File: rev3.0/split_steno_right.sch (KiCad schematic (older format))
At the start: 37 parts, among them J1 USB_B, J2 Audio-Jack-4, J3 Conn_02x04_Odd_Even, J4 Conn_01x03, J5 Conn_01x03, J6 Conn_01x02, P1 TC2030-IDC, SW1 SW_Push, SW10 SW_Push, SW11 SW_Push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

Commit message: filled gnd plane on left
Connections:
- net KEY1: no longer U2.24 (PD4/OC1A/~SS~)
- net KEY10: no longer U2.43 (AC3/ADC3/PA3)
- net KEY11: no longer U2.11 (SCLIN/SCL/XCK0/OC0AHS/OC0B/PC1)
- net KEY12: no longer U2.10 (SDAIN/SDA/~OC0ALS~/OC0A/PC0)
- net KEY13: no longer U2.3 (AC0OUT/AC7/ADC7/PA7)
- net KEY14: no longer U2.2 (AC1OUT/AC6/ADC6/PA6)
- net KEY15: no longer U2.44 (AC4/ADC4/PA4)
- net KEY16: no longer U2.5 (ADC9/PB1)
- net KEY17: no longer U2.4 (AREFB/ADC8/PB0)
- net KEY18: no longer U2.1 (AC5/ADC5/PA5)
- net KEY2: no longer U2.25 (PD5/OC1B/XCK1/MOSI)
- net KEY3: no longer U2.33 (PE3/OC0D/TXD0)
- net KEY4: no longer U2.36 (PR0/XTAL2/TOSC2)
- net KEY5: no longer U2.42 (AC2/ADC2/PA2)
- net KEY6: no longer U2.23 (PD3/OC0D/TXD0)
- net KEY7: no longer U2.20 (PD0/OC0A)
- net KEY8: no longer U2.32 (PE2/OC0C/RXD0)
- net KEY9: no longer U2.41 (AC1/ADC1/PA1)
- net SCL: now also U2.11 (SCLIN/SCL/XCK0/OC0AHS/OC0B/PC1); no longer U2.29 (PE1/OC0B/XCK0/SCL)
- net SDA: now also U2.10 (SDAIN/SDA/~OC0ALS~/OC0A/PC0); no longer U2.28 (PE0/OC0A/SDA)
- net EXTRA1: no longer names the net of U2.22 (PD2/OC0C/RXD0)
- net EXTRA1: no longer J5.2 (Pin_2)
- net EXTRA2: no longer names the net of U2.37 (PR1/XTAL1/TOSC1)
- net EXTRA2: no longer J6.1 (Pin_1)
- net UNDER_RGB: no longer names the net of U2.6 (DAC0/ADC10/PB2)
- net UNDER_RGB: no longer J4.2 (Pin_2)
- no-connect marks 6 -> 4
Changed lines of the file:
@@
 EESchema Schematic File Version 2
-LIBS:atmel
-LIBS:bus_switches
-LIBS:conn_usb
-LIBS:kicad_util
-LIBS:logic
-LIBS:microchip
-LIBS:nordic
-LIBS:nordic2
-LIBS:onsemi
-LIBS:rgb_led
-LIBS:silabs
-LIBS:switch
-LIBS:Tag-Connect
-LIBS:power
-LIBS:device
-LIBS:switches
-LIBS:relays
-LIBS:motors
-LIBS:transistors
-LIBS:conn
-LIBS:linear
-LIBS:regul
-LIBS:74xx
-LIBS:cmos4000
-LIBS:adc-dac
-LIBS:memory
-LIBS:xilinx
-LIBS:microcontrollers
-LIBS:dsp
-LIBS:analog_switches
-LIBS:motorola
-LIBS:texas
-LIBS:intel
-LIBS:audio
-LIBS:interface
-LIBS:digital-audio
-LIBS:philips
-LIBS:display
-LIBS:cypress
-LIBS:siliconi
-LIBS:opto
-LIBS:contrib
-LIBS:valves
-LIBS:split_steno_left-cache
+LIBS:split_steno_right
 EELAYER 25 0
 EELAYER END
@@
 Text Label 7975 2375 2    60   ~ 0
 PDI
-Text Label 7975 3025 2    60   ~ 0
+Text Label 9775 3475 0    60   ~ 0
 SDA
-Text Label 7975 3125 2    60   ~ 0
+Text Label 9775 3575 0    60   ~ 0
 SCL
 $Comp
@@
 Connection ~ 3700 1675
 Connection ~ 3700 1450
-Wire Wire Line
-	7975 3025 7075 3025
-Wire Wire Line
-	7975 3125 7075 3125
 Connection ~ 7400 3025
 Connection ~ 7225 3125
@@
 	1    0    0    -1
 $EndComp
-Text Label 9775 3575 0    60   ~ 0
-KEY11
-Text Label 9775 3475 0    60   ~ 0
-KEY12
-Text Label 9775 2575 0    60   ~ 0
-KEY15
-Text Label 9775 2775 0    60   ~ 0
-KEY14
-Text Label 9775 2875 0    60   ~ 0
-KEY13
-Text Label 9775 2675 0    60   ~ 0
-KEY18
-Text Label 9775 3025 0    60   ~ 0
-KEY17
-Text Label 9775 3125 0    60   ~ 0
-KEY16
-Text Label 9775 3225 0    60   ~ 0
-UNDER_RGB
-Text Label 5775 3525 2    60   ~ 0
-UNDER_RGB
-Text Label 7975 3475 2    60   ~ 0
-KEY7
-Text Label 7975 3775 2    60   ~ 0
-KEY6
-Text Label 7975 3875 2    60   ~ 0
-KEY1
-Text Label 7975 3975 2    60   ~ 0
-KEY2
-Text Label 7975 3325 2    60   ~ 0
-KEY3
-Text Label 7975 2775 2    60   ~ 0
-KEY4
-Text Label 7975 3225 2    60   ~ 0
-KEY8
-Text Label 9775 2275 0    60   ~ 0
-KEY9
-Text Label 9775 2375 0    60   ~ 0
-KEY5
-Text Label 9775 2475 0    60   ~ 0
-KEY10
-Text Label 7975 2875 2    60   ~ 0
-EXTRA2
-Text Label 7975 3675 2    60   ~ 0
-EXTRA1
 NoConn ~ 7975 3575
-NoConn ~ 9775 2175
-NoConn ~ 9775 3325
-Text Label 5775 4100 2    60   ~ 0
-EXTRA1
-Text Label 5775 4500 2    60   ~ 0
-EXTRA2
 $Comp
 L Conn_01x03 J4
@@
 	0    1    1    0
 $EndComp
+Text Label 7550 3025 0    60   ~ 0
+SDA
+Text Label 7550 3125 0    60   ~ 0
+SCL
+Wire Wire Line
+	7075 3025 7550 3025
+Wire Wire Line
+	7075 3125 7550 3125
 $EndSCHEMATC

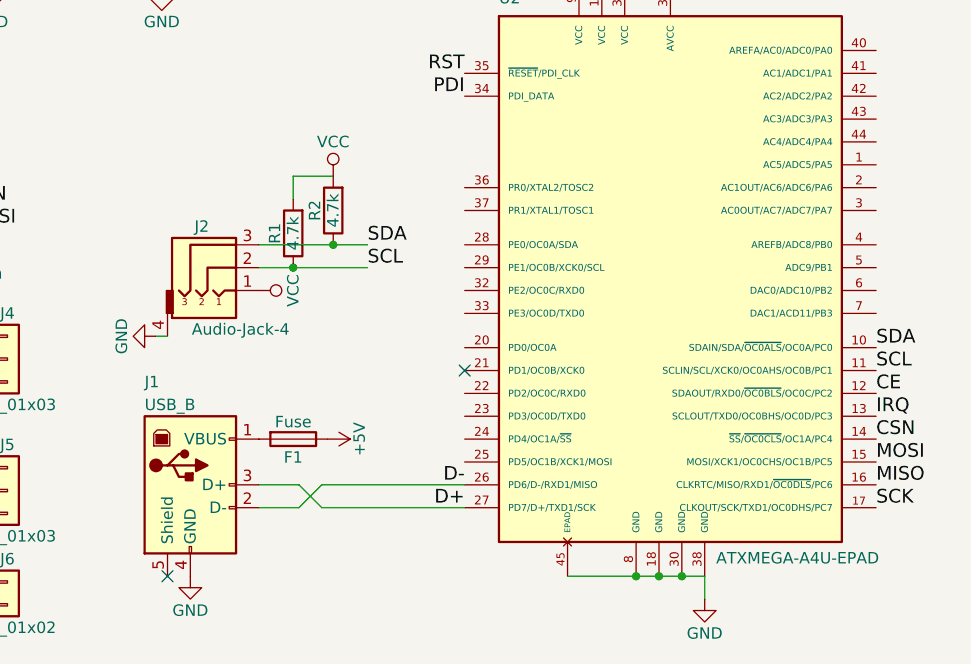
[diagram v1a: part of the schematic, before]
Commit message: redid right hand side positions to match left hand
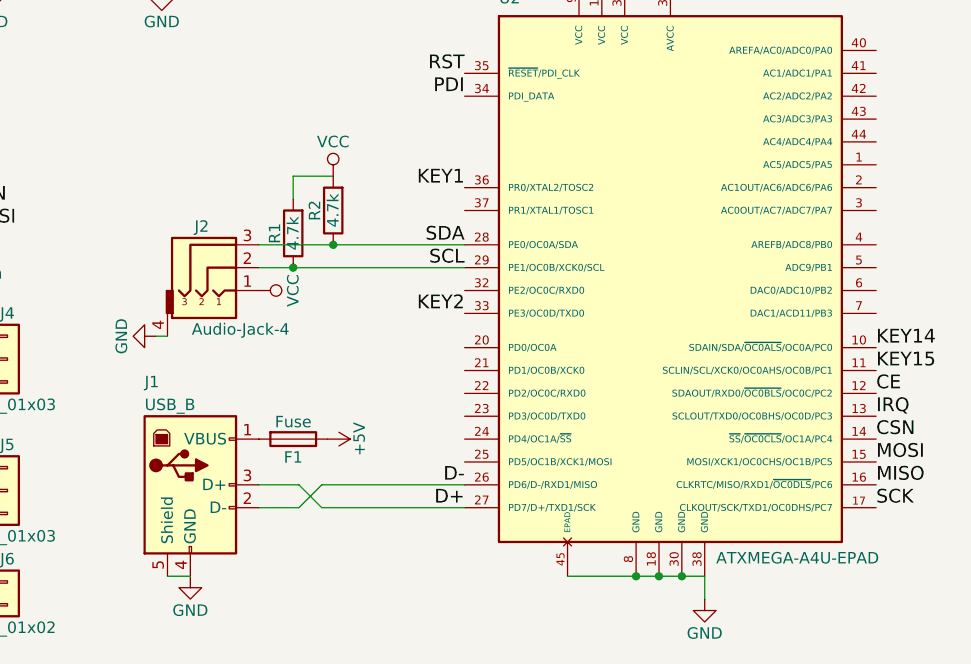
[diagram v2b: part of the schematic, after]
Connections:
- net GND: now also J1.5 (Shield)
- net KEY1: now also U2.36 (PR0/XTAL2/TOSC2)
- net KEY14: now also U2.10 (SDAIN/SDA/~OC0ALS~/OC0A/PC0)
- net KEY15: now also U2.11 (SCLIN/SCL/XCK0/OC0AHS/OC0B/PC1)
- net KEY2: now also U2.33 (PE3/OC0D/TXD0)
- net SCL: now also U2.29 (PE1/OC0B/XCK0/SCL); no longer U2.11 (SCLIN/SCL/XCK0/OC0AHS/OC0B/PC1)
- net SDA: now also U2.28 (PE0/OC0A/SDA); no longer U2.10 (SDAIN/SDA/~OC0ALS~/OC0A/PC0)
- no-connect marks 4 -> 2
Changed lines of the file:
@@
 EESchema Schematic File Version 2
 LIBS:split_steno_right
+LIBS:split_steno_right-cache
 EELAYER 25 0
 EELAYER END
@@
 Text Label 7975 4075 2    60   ~ 0
 D-
-NoConn ~ 6675 4475
 $Comp
 L Fuse F1
@@
 Text Label 7975 2375 2    60   ~ 0
 PDI
-Text Label 9775 3475 0    60   ~ 0
-SDA
-Text Label 9775 3575 0    60   ~ 0
-SCL
 $Comp
 L R R1
@@
 	1    0    0    -1
 $EndComp
-NoConn ~ 7975 3575
 $Comp
 L Conn_01x03 J4
@@
 	0    1    1    0
 $EndComp
-Text Label 7550 3025 0    60   ~ 0
+Text Label 7975 3025 2    60   ~ 0
 SDA
-Text Label 7550 3125 0    60   ~ 0
+Text Label 7975 3125 2    60   ~ 0
 SCL
 Wire Wire Line
-	7075 3025 7550 3025
-Wire Wire Line
-	7075 3125 7550 3125
+	7075 3025 7975 3025
+Wire Wire Line
+	7075 3125 7975 3125
+Text Label 9775 3475 0    60   ~ 0
+KEY14
+Text Label 9775 3575 0    60   ~ 0
+KEY15
+Text Label 7975 3325 2    60   ~ 0
+KEY2
+Text Label 7975 2775 2    60   ~ 0
+KEY1
+Wire Wire Line
+	6675 4475 6775 4475
 $EndSCHEMATC

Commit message: finished right hand
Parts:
- removed J4, J5: Conn_01x03, lib_fp:Pin_Header_Straight_1x03_Pitch2.54mm, symbol Conn_01x03
- added J5: Conn_02x04_Odd_Even, lib_fp:Pin_Header_Straight_2x04_Pitch2.54mm, symbol Conn_02x04_Odd_Even
- renumbered J6 to J4
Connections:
- net GND: now also J5.1 (Pin_1)
- net KEY10: now also U2.21 (PD1/OC0B/XCK0)
- net KEY11: now also U2.1 (AC5/ADC5/PA5)
- net KEY12: now also U2.3 (AC0OUT/AC7/ADC7/PA7)
- net KEY13: now also U2.6 (DAC0/ADC10/PB2)
- net KEY16: now also U2.4 (AREFB/ADC8/PB0)
- net KEY17: now also U2.5 (ADC9/PB1)
- net KEY18: now also U2.7 (DAC1/ACD11/PB3)
- net KEY3: now also U2.25 (PD5/OC1B/XCK1/MOSI)
- net KEY4: now also U2.24 (PD4/OC1A/~SS~)
- net KEY5: now also U2.22 (PD2/OC0C/RXD0)
- net KEY6: now also U2.2 (AC1OUT/AC6/ADC6/PA6)
- net KEY7: now also U2.32 (PE2/OC0C/RXD0)
- net KEY8: now also U2.20 (PD0/OC0A)
- net KEY9: now also U2.23 (PD3/OC0D/TXD0)
- net VCC: now also J5.2 (Pin_2)
- net EXTRA1: now reaches U2.37 (PR1/XTAL1/TOSC1)
- net EXTRA1: now also J4.1 (Pin_1)
- net EXTRA2: now reaches U2.40 (AREFA/AC0/ADC0/PA0)
- net EXTRA2: now also J5.4 (Pin_4)
- net EXTRA3: now reaches U2.41 (AC1/ADC1/PA1)
- net EXTRA3: now also J5.3 (Pin_3)
- net EXTRA4: now reaches U2.42 (AC2/ADC2/PA2)
- net EXTRA4: now also J5.6 (Pin_6)
- net EXTRA5: now reaches U2.43 (AC3/ADC3/PA3)
- net EXTRA5: now also J5.5 (Pin_5)
- net EXTRA6: now reaches U2.44 (AC4/ADC4/PA4)
- net EXTRA6: now also J5.8 (Pin_8)
- no-connect marks 2 -> 3
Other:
- moved on the sheet: J4
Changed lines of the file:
@@
 $EndComp
 $Comp
-L Conn_01x03 J4
-U 1 1 5B15D849
-P 5975 3525
-F 0 "J4" H 5975 3725 50  0000 C CNN
-F 1 "Conn_01x03" H 5975 3325 50  0000 C CNN
-F 2 "lib_fp:Pin_Header_Straight_1x03_Pitch2.54mm" H 5975 3525 50  0001 C CNN
-F 3 "" H 5975 3525 50  0001 C CNN
-	1    5975 3525
+L Conn_01x02 J4
+U 1 1 5B15E1F9
+P 6075 3475
+F 0 "J4" H 6075 3575 50  0000 C CNN
+F 1 "Conn_01x02" H 6075 3275 50  0000 C CNN
+F 2 "lib_fp:Pin_Header_Straight_1x02_Pitch2.54mm" H 6075 3475 50  0001 C CNN
+F 3 "" H 6075 3475 50  0001 C CNN
+	1    6075 3475
 	1    0    0    -1
 $EndComp
 $Comp
-L VCC #PWR024
-U 1 1 5B15DA49
-P 5775 3425
-F 0 "#PWR024" H 5775 3275 50  0001 C CNN
-F 1 "VCC" H 5775 3575 50  0000 C CNN
-F 2 "" H 5775 3425 50  0001 C CNN
-F 3 "" H 5775 3425 50  0001 C CNN
-	1    5775 3425
-	1    0    0    -1
-$EndComp
-$Comp
-L GND #PWR025
-U 1 1 5B15DAC3
-P 5775 3625
-F 0 "#PWR025" H 5775 3375 50  0001 C CNN
-F 1 "GND" H 5775 3475 50  0000 C CNN
-F 2 "" H 5775 3625 50  0001 C CNN
-F 3 "" H 5775 3625 50  0001 C CNN
-	1    5775 3625
-	0    1    1    0
-$EndComp
-$Comp
-L Conn_01x03 J5
-U 1 1 5B15DE45
-P 5975 4100
-F 0 "J5" H 5975 4300 50  0000 C CNN
-F 1 "Conn_01x03" H 5975 3900 50  0000 C CNN
-F 2 "lib_fp:Pin_Header_Straight_1x03_Pitch2.54mm" H 5975 4100 50  0001 C CNN
-F 3 "" H 5975 4100 50  0001 C CNN
-	1    5975 4100
-	1    0    0    -1
-$EndComp
-$Comp
-L VCC #PWR026
-U 1 1 5B15E01D
-P 5775 4000
-F 0 "#PWR026" H 5775 3850 50  0001 C CNN
-F 1 "VCC" H 5775 4150 50  0000 C CNN
-F 2 "" H 5775 4000 50  0001 C CNN
-F 3 "" H 5775 4000 50  0001 C CNN
-	1    5775 4000
-	1    0    0    -1
-$EndComp
-$Comp
-L GND #PWR027
-U 1 1 5B15E097
-P 5775 4200
-F 0 "#PWR027" H 5775 3950 50  0001 C CNN
-F 1 "GND" H 5775 4050 50  0000 C CNN
-F 2 "" H 5775 4200 50  0001 C CNN
-F 3 "" H 5775 4200 50  0001 C CNN
-	1    5775 4200
-	0    1    1    0
-$EndComp
-$Comp
-L Conn_01x02 J6
-U 1 1 5B15E1F9
-P 5975 4500
-F 0 "J6" H 5975 4600 50  0000 C CNN
-F 1 "Conn_01x02" H 5975 4300 50  0000 C CNN
-F 2 "lib_fp:Pin_Header_Straight_1x02_Pitch2.54mm" H 5975 4500 50  0001 C CNN
-F 3 "" H 5975 4500 50  0001 C CNN
-	1    5975 4500
-	1    0    0    -1
-$EndComp
-$Comp
-L GND #PWR028
+L GND #PWR024
 U 1 1 5B15E563
-P 5775 4600
-F 0 "#PWR028" H 5775 4350 50  0001 C CNN
-F 1 "GND" H 5775 4450 50  0000 C CNN
-F 2 "" H 5775 4600 50  0001 C CNN
-F 3 "" H 5775 4600 50  0001 C CNN
-	1    5775 4600
+P 5875 3575
+F 0 "#PWR024" H 5875 3325 50  0001 C CNN
+F 1 "GND" H 5875 3425 50  0000 C CNN
+F 2 "" H 5875 3575 50  0001 C CNN
+F 3 "" H 5875 3575 50  0001 C CNN
+	1    5875 3575
 	0    1    1    0
 $EndComp
@@
 Wire Wire Line
 	6675 4475 6775 4475
+Text Label 9775 3325 0    60   ~ 0
+KEY18
+Text Label 9775 3225 0    60   ~ 0
+KEY13
+Text Label 9775 3025 0    60   ~ 0
+KEY16
+Text Label 9775 3125 0    60   ~ 0
+KEY17
+Text Label 9775 2675 0    60   ~ 0
+KEY11
+Text Label 9775 2875 0    60   ~ 0
+KEY12
+Text Label 7975 3225 2    60   ~ 0
+KEY7
+Text Label 9775 2775 0    60   ~ 0
+KEY6
+Text Label 7975 3975 2    60   ~ 0
+KEY3
+Text Label 7975 3875 2    60   ~ 0
+KEY4
+Text Label 7975 3775 2    60   ~ 0
+KEY9
+Text Label 7975 3675 2    60   ~ 0
+KEY5
+Text Label 7975 3575 2    60   ~ 0
+KEY10
+Text Label 7975 3475 2    60   ~ 0
+KEY8
+$Comp
+L Conn_02x04_Odd_Even J5
+U 1 1 5B20101F
+P 5525 4175
+F 0 "J5" H 5575 4375 50  0000 C CNN
+F 1 "Conn_02x04_Odd_Even" H 5575 3875 50  0000 C CNN
+F 2 "lib_fp:Pin_Header_Straight_2x04_Pitch2.54mm" H 5525 4175 50  0001 C CNN
+F 3 "" H 5525 4175 50  0001 C CNN
+	1    5525 4175
+	1    0    0    -1
+$EndComp
+$Comp
+L VCC #PWR025
+U 1 1 5B20121B
+P 5825 4075
+F 0 "#PWR025" H 5825 3925 50  0001 C CNN
+F 1 "VCC" H 5825 4225 50  0000 C CNN
+F 2 "" H 5825 4075 50  0001 C CNN
+F 3 "" H 5825 4075 50  0001 C CNN
+	1    5825 4075
+	1    0    0    -1
+$EndComp
+$Comp
+L GND #PWR026
+U 1 1 5B2012E4
+P 5325 4075
+F 0 "#PWR026" H 5325 3825 50  0001 C CNN
+F 1 "GND" H 5325 3925 50  0000 C CNN
+F 2 "" H 5325 4075 50  0001 C CNN
+F 3 "" H 5325 4075 50  0001 C CNN
+	1    5325 4075
+	-1   0    0    1
+$EndComp
+Text Label 5875 3475 2    60   ~ 0
+EXTRA1
+Text Label 7975 2875 2    60   ~ 0
+EXTRA1
+Text Label 9775 2175 0    60   ~ 0
+EXTRA2
+Text Label 9775 2275 0    60   ~ 0
+EXTRA3
+Text Label 9775 2375 0    60   ~ 0
+EXTRA4
+Text Label 9775 2475 0    60   ~ 0
+EXTRA5
+Text Label 9775 2575 0    60   ~ 0
+EXTRA6
+Text Label 5825 4175 0    60   ~ 0
+EXTRA2
+Text Label 5325 4175 2    60   ~ 0
+EXTRA3
+Text Label 5825 4275 0    60   ~ 0
+EXTRA4
+Text Label 5325 4275 2    60   ~ 0
+EXTRA5
+Text Label 5825 4375 0    60   ~ 0
+EXTRA6
+NoConn ~ 5325 4375
 $EndSCHEMATC
